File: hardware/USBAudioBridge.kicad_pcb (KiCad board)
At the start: 4 copper layers, 43.2 x 62 mm, 120 parts, among them J101 USB_C_Receptacle, J501 SWD, J502 UART, J601 PMOD_JB, J602 PMOD_JC, Q401 BSS84, SW301 RESET, SW401 BOOT, U1 MIMXRT1011DAE5A, U101 USBLC6-2SC6, U102 AP7361C-33E, U103 LP5907MFX-3.3, U301 MCP120T-300I/TT, U401 W25Q128JVSIQ, U601 CDCV304PW, X601 24.576MHz, Y301 24MHz, Y302 32.768kHz

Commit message: finish second pcb layout revision
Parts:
- C201, C202, C301, C302, C303, C304, C305, C306, C307, L201, R301, R302, U1, U301, Y301, Y302: moved to B.Cu
- C203, C204, C205, C206, C207, C208, C209, C210, C211, C213, C214, C215, C216, C217, C218, C219, C220, C221, C222, C223, C224, C225, C226, C227, C228, C229, C230: moved to F.Cu
- J501: footprint Connector_PinHeader_1.27mm:PinHeader_2x05_P1.27mm_Vertical_SMD -> USBAudioBridge:Samtec_FTSH-105-01-L-DV-K
- moved J501 34.9 mm to (139.4, 125.6), turned to 0 degrees
- moved C202 34.3 mm to (105.6, 122.2), turned to -90 degrees
- moved C306 32.9 mm to (109.8, 113.4), turned to 0 degrees
- moved C201 31.8 mm to (105.6, 119.2)
- moved C307 31.8 mm to (112.4, 115.8)
- moved R302 31.8 mm to (112.4, 113.4)
- moved U301 29.7 mm to (109.8, 116.0), turned to 0 degrees
- moved R502 25.5 mm to (134.4, 129.4)
- moved R501 25.2 mm to (134.4, 122.0)
- moved C208 25.2 mm to (109.7, 127.2), turned to 180 degrees
- moved C211 24.6 mm to (109.7, 121.7), turned to 180 degrees
- moved L201 24.4 mm to (109.6, 121.4)
- moved C223 23.8 mm to (133.5, 123.5), turned to 0 degrees
- moved C209 23.8 mm to (109.7, 124.2), turned to 180 degrees
- moved C222 23.8 mm to (133.5, 124.7), turned to 0 degrees
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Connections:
- net /Audio Clock & PMOD/JC_TX_BCLK renamed /Audio Clock & PMOD/JC_GPIO0
- net /Audio Clock & PMOD/JC_TX_DATA renamed /Audio Clock & PMOD/JC_GPIO1
- net /Audio Clock & PMOD/JC_TX_LRCLK renamed /Audio Clock & PMOD/JC_RST
- J601 pad 1: /Audio Clock & PMOD/JB_SPI_CS -> /Audio Clock & PMOD/JB_RX_MCLK
- J601 pad 10: /Audio Clock & PMOD/JB_GPIO1 -> /Audio Clock & PMOD/JB_TX_DATA
- J601 pad 2: /Audio Clock & PMOD/JB_SPI_MOSI -> /Audio Clock & PMOD/JB_RX_LRCLK
- J601 pad 3: /Audio Clock & PMOD/JB_SPI_MISO -> /Audio Clock & PMOD/JB_RX_BCLK
- J601 pad 4: /Audio Clock & PMOD/JB_SPI_SCK -> /Audio Clock & PMOD/JB_RX_DATA
- J601 pad 7: /Audio Clock & PMOD/JB_INT -> /Audio Clock & PMOD/JB_TX_MCLK
- J601 pad 8: /Audio Clock & PMOD/JB_RST -> /Audio Clock & PMOD/JB_TX_LRCLK
- J601 pad 9: /Audio Clock & PMOD/JB_GPIO0 -> /Audio Clock & PMOD/JB_TX_BCLK
- J602 pad 1: /Audio Clock & PMOD/JC_RX_MCLK -> /Audio Clock & PMOD/JC_SPI_CS
- J602 pad 2: /Audio Clock & PMOD/JC_RX_LRCLK -> /Audio Clock & PMOD/JC_SPI_MOSI
- J602 pad 3: /Audio Clock & PMOD/JC_RX_BCLK -> /Audio Clock & PMOD/JC_SPI_MISO
- J602 pad 4: /Audio Clock & PMOD/JC_RX_DATA -> /Audio Clock & PMOD/JC_SPI_SCK
- J602 pad 7: /Audio Clock & PMOD/JC_TX_MCLK -> /Audio Clock & PMOD/JC_INT
- R604 pad 2: /Audio Clock & PMOD/JC_RX_MCLK -> /Audio Clock & PMOD/JB_RX_MCLK
- R605 pad 2: /Audio Clock & PMOD/JC_TX_MCLK -> /Audio Clock & PMOD/JB_TX_MCLK
- R606 pad 1: SPI_CS -> I2S_RX_LRCLK
- R606 pad 2: /Audio Clock & PMOD/JB_SPI_CS -> /Audio Clock & PMOD/JB_RX_LRCLK
- R607 pad 1: SPI_MOSI -> I2S_RX_BCLK
- R607 pad 2: /Audio Clock & PMOD/JB_SPI_MOSI -> /Audio Clock & PMOD/JB_RX_BCLK
- R608 pad 1: SPI_MISO -> I2S_RX_DATA
- R608 pad 2: /Audio Clock & PMOD/JB_SPI_MISO -> /Audio Clock & PMOD/JB_RX_DATA
- R609 pad 1: SPI_SCK -> /Audio Clock & PMOD/JB_TX_LRCLK
- R609 pad 2: /Audio Clock & PMOD/JB_SPI_SCK -> I2S_TX_LRCLK
- R610 pad 1: /Audio Clock & PMOD/JB_INT -> /Audio Clock & PMOD/JB_TX_BCLK
- R610 pad 2: PMOD_INT -> I2S_TX_BCLK
- R611 pad 1: /Audio Clock & PMOD/JB_RST -> /Audio Clock & PMOD/JB_TX_DATA
- R611 pad 2: PMOD_RST -> I2S_TX_DATA
- R612 pad 1: /Audio Clock & PMOD/JB_GPIO0 -> SPI_CS
- R612 pad 2: PMOD_GPIO0 -> /Audio Clock & PMOD/JC_SPI_CS
- R613 pad 1: /Audio Clock & PMOD/JB_GPIO1 -> SPI_MOSI
- R613 pad 2: PMOD_GPIO1 -> /Audio Clock & PMOD/JC_SPI_MOSI
- R614 pad 1: I2S_RX_LRCLK -> SPI_MISO
- R614 pad 2: /Audio Clock & PMOD/JC_RX_LRCLK -> /Audio Clock & PMOD/JC_SPI_MISO
- R615 pad 1: I2S_RX_BCLK -> SPI_SCK
- R615 pad 2: /Audio Clock & PMOD/JC_RX_BCLK -> /Audio Clock & PMOD/JC_SPI_SCK
- R616 pad 1: I2S_RX_DATA -> /Audio Clock & PMOD/JC_INT
- R616 pad 2: /Audio Clock & PMOD/JC_RX_DATA -> PMOD_INT
- R617 pad 2: I2S_TX_LRCLK -> PMOD_RST
- R618 pad 2: I2S_TX_BCLK -> PMOD_GPIO0
- R619 pad 2: I2S_TX_DATA -> PMOD_GPIO1
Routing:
- net Net-(U601-1Y2): track 16.1 -> 38.0 mm
- net SPI_MISO: track 32.6 -> 53.3 mm, vias 2 -> 3
- net MCLK_SAI: track 13.2 -> 33.5 mm, vias 0 -> 1
- net +5V: track 113.2 -> 95.4 mm
- net Net-(U601-1Y3): track 16.4 -> 33.3 mm
- net /USB-C & Power/CC1: track 4.60 -> 20.6 mm
- net FLASH_IO1: track 24.6 -> 9.04 mm, vias 1 -> 0
- net UART_RX: track 37.4 -> 51.8 mm, vias 2 -> 1
- net XTALO: track 19.2 -> 7.33 mm
- net JTAG_MOD: track 11.8 -> 23.3 mm, vias 0 -> 1
- net VBUS: track 34.4 -> 23.3 mm, vias 2 -> 4
- net POR_B: track 58.4 -> 69.2 mm, vias 2 -> 1
- net +3V3_CLK: track 74.1 -> 63.9 mm, vias 2 -> 0
- net I2S_TX_LRCLK: track 24.1 -> 34.1 mm, vias 0 -> 1
- net /Audio Clock & PMOD/JB_TX_MCLK: track 0.00 -> 9.81 mm
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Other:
- board text added: "JC: SPI+GPIO JB: I2S (Pmod I2S2)"
- board text added: "USB Audio Bridge v1.0"
- board text removed: "JC: I2S (Pmod I2S2) JB: SPI+GPIO"
- board text removed: "USB Audio Bridge rev A"

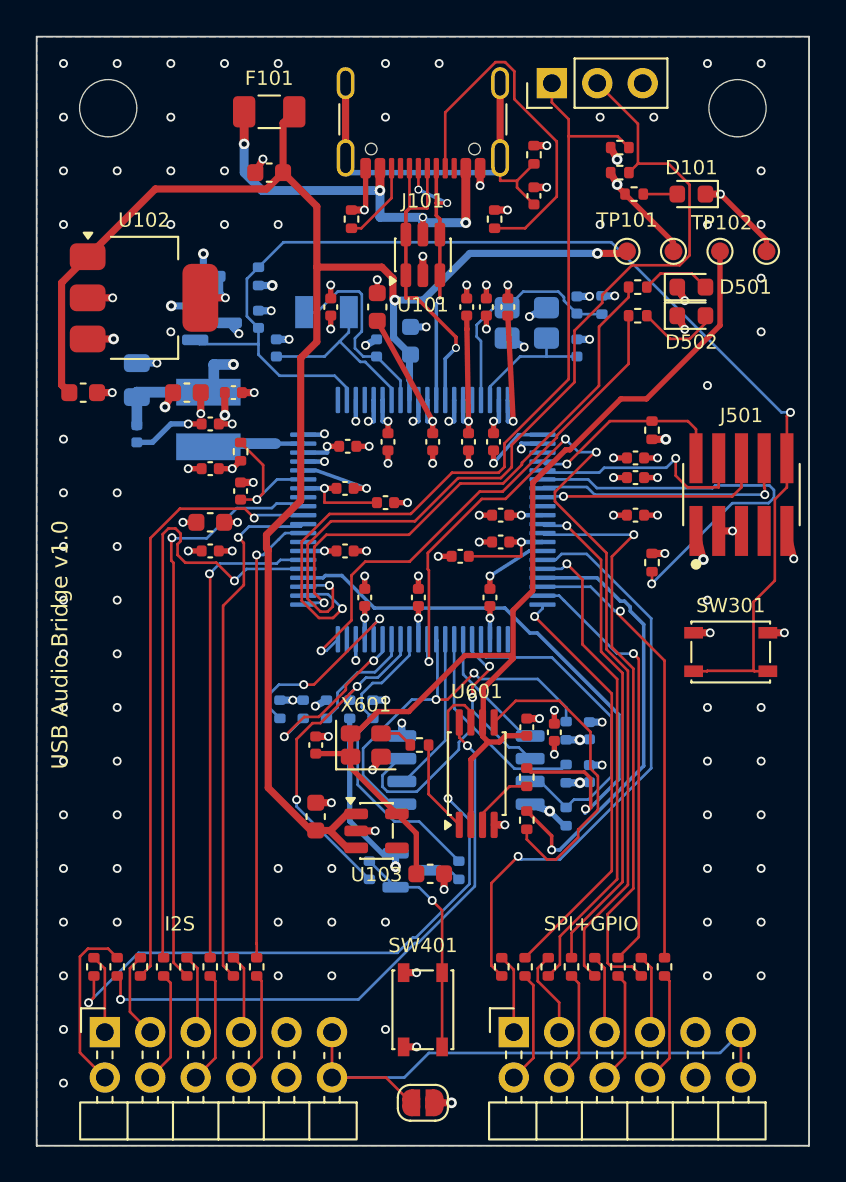
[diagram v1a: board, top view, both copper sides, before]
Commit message: Add fab pipeline, sourcing, CI and developer reference manual
- tools/fab.py: ERC/DRC gate, then JLCPCB (LCSC BOM, rotation-corrected
  CPL) and PCBWay (MPN BOM, centroid) packages with Gerbers, drill,
  assembly drawings, schematic PDF and order notes
- .github/workflows/fab.yml: runs fab.py in kicad/kicad:10.0.7; artifacts
  on push/PR, release assets on v* tags
- design.py: MPN/Manufacturer/LCSC for every BOM line (checked against
  JLCPCB stock); SG-210SCBA oscillator, Liming 200 uW 24 MHz crystal,
  PTS810SJG switches, USB4105-GF-A-120, ~2 V LEDs
- R603 DNP: GPT2 cannot count 24.576 MHz (external clock < PERCLK/4,
  PERCLK <= 75 MHz); async feedback comes from SAI sample counts
- Via drill 0.3 -> 0.2 mm (pads unchanged) for PCBWay's 5 mil ring
- Drill/place origin at the board's lower-left corner; legible Fab refs
- pcb.py --sync-fields updates fields/DNP without re-routing
- docs/reference-manual.md: RT1010 firmware and Arty A7 reference
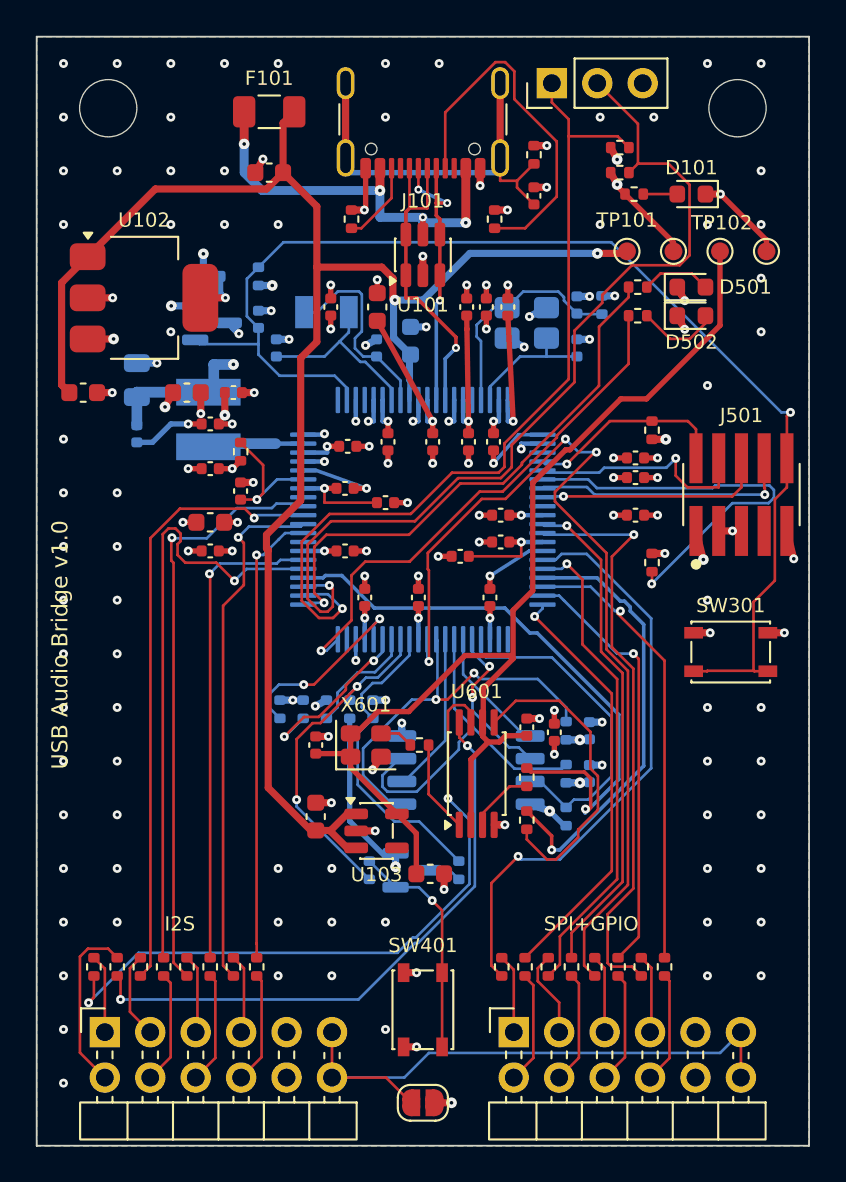
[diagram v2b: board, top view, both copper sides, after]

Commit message: improve manufacturability
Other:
- board text added: "0V"
- board text added: "3V"
- board text added: "5V"
- board text added: "CK"
- board text added: "Hold BOOT, tap RESET: USB boot"
- board text removed: "Hold BOOT + tap RESET = USB serial downloader"
